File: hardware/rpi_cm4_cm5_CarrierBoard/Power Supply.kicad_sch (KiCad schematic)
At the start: 94 parts, among them Q19 2N7002, Q2 2N7002, Q20 2N7002, Q22 SSM3K56FS,LF, Q23 SSM3K56FS,LF, Q24 2N7002, Q3 2N7002, Q7 2N7002, U10 TPS54527DDAR, U11 TPS54527DDAR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

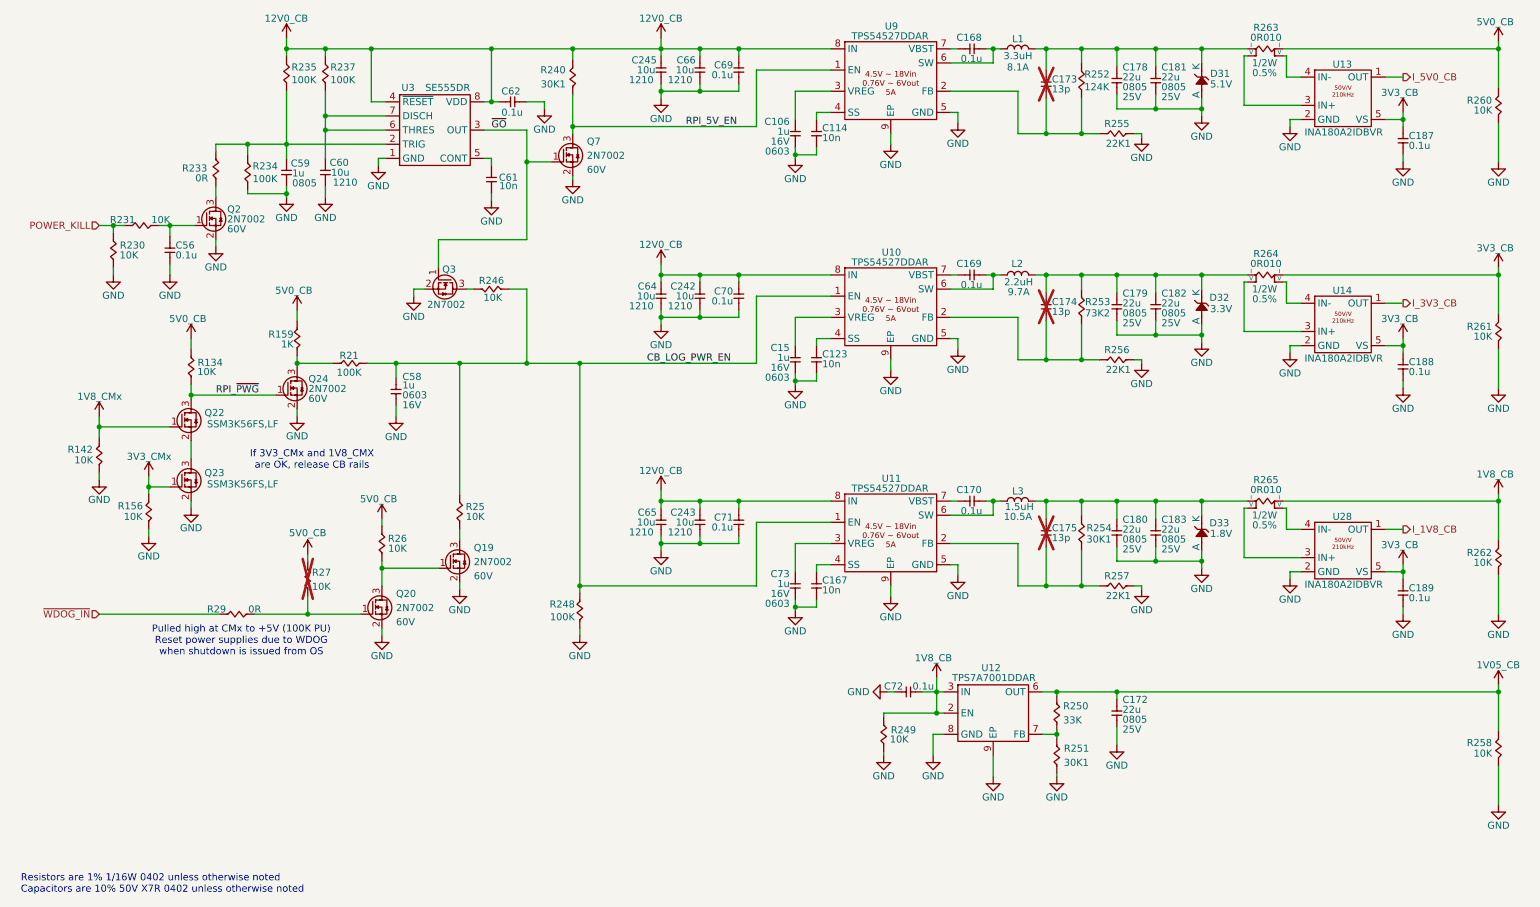
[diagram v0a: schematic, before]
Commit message: Add test points on relevant signals Re-generate SCH_PDF Re-generate BOM Re-generate all gerbers and relevant PCB output files (still in review phase)
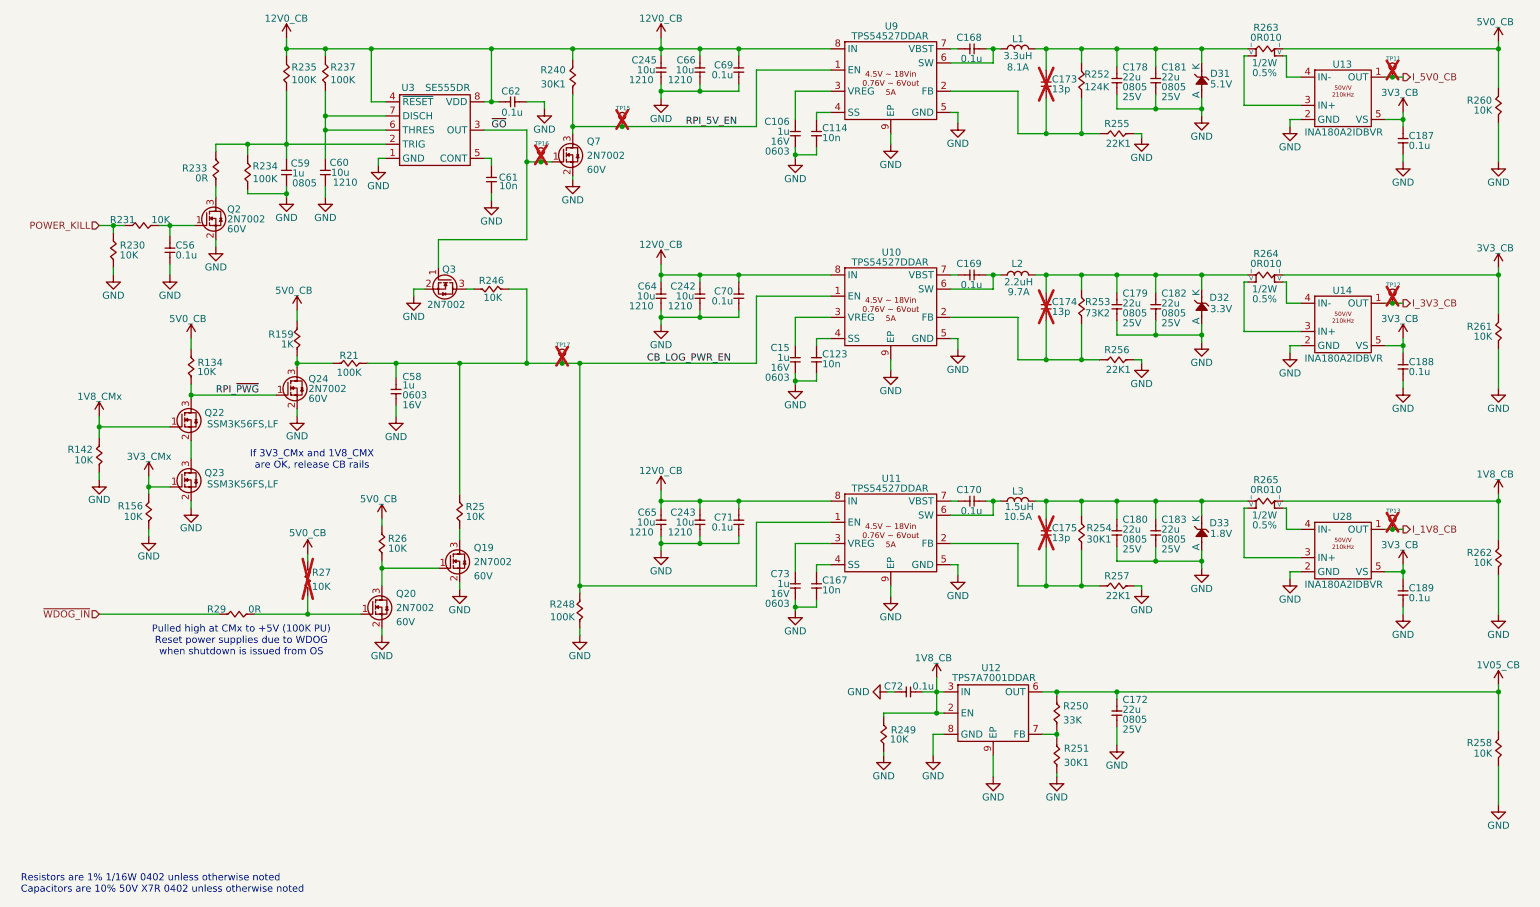
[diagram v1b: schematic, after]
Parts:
- added TP11, TP12, TP13, TP15, TP16, TP17: 28 mils, footprint:SMT_TP_28_MILS, symbol KicadCompDb:Test Point/TP_00001
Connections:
- net CB_LOG_PWR_EN: now also TP17.1
- net I_1V8_CB: now also TP13.1
- net I_3V3_CB: now also TP12.1
- net I_5V0_CB: now also TP11.1
- net RPI_5V_EN: now also TP15.1
- net ~{GO}: now also TP16.1
